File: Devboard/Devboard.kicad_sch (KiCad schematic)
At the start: 49 parts, among them IC1 114993390, J1 693071010811, J2 USB_C_Receptacle_USB2.0_16P, J3 SWD, J4 RMF, J5 RMF, SW1 SHPHLD, SW2 SW_Push, SW3 RST, U1 NPM1304-QEAA-R, U2 E73-2G4M08S1C, U3 SRV05-4, Y1 32.768

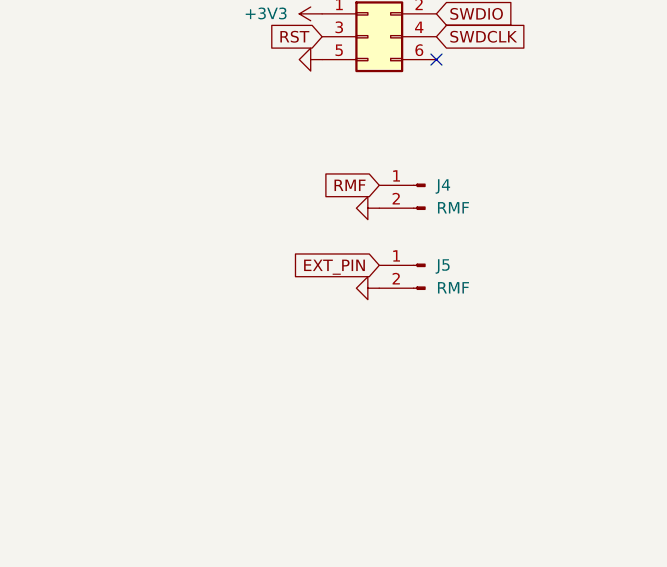
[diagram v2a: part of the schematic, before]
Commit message: Added 3V3 output
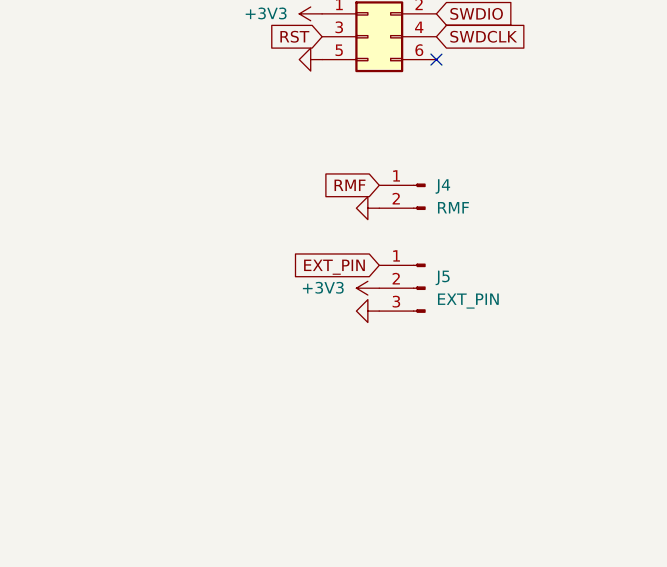
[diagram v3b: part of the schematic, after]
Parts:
- removed J5: RMF, Connector_PinHeader_2.54mm:PinHeader_1x02_P2.54mm_Vertical, symbol Connector:Conn_01x02_Pin
- added J5: EXT_PIN, Connector_PinHeader_2.54mm:PinHeader_1x03_P2.54mm_Vertical, symbol Connector:Conn_01x03_Pin
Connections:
- net +3V3: now also J5.2 (Pin_2)
- net EXT_PIN: now also J5.1 (Pin_1)
- net GND: now also J5.3 (Pin_3)
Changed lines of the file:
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@@
+	)
+	(symbol
+		(lib_id "power:+3.3V")
+		(at 372.11 142.24 90)
+		(unit 1)
+		(body_style 1)
+		(exclude_from_sim no)
+		(in_bom yes)
+		(on_board yes)
+		(in_pos_files yes)
+		(dnp no)
+		(fields_autoplaced yes)
+		(property "Reference" "#PWR048"
+			(at 375.92 142.24 0)
+			(hide yes)
+			(show_name no)
+			(do_not_autoplace no)
+			(effects
+				(font
+					(size 1.27 1.27)
+				)
+			)
+		)
+		(property "Value" "+3V3"
+			(at 368.3 142.2399 90)
+			(show_name no)
+			(do_not_autoplace no)
+			(effects
+				(font
+					(size 1.27 1.27)
+				)
+				(justify left)
+			)
+		)
+		(property "Footprint" ""
+			(at 372.11 142.24 0)
+			(hide yes)
+			(show_name no)
+			(do_not_autoplace no)
+			(effects
+				(font
+					(size 1.27 1.27)
+				)
+			)
+		)
+		(property "Datasheet" ""
+			(at 372.11 142.24 0)
+			(hide yes)
+			(show_name no)
+			(do_not_autoplace no)
+			(effects
+				(font
+					(size 1.27 1.27)
+				)
+			)
+		)
+		(property "Description" "Power symbol creates a global label with name \"+3.3V\""
+			(at 372.11 142.24 0)
+			(hide yes)
+			(show_name no)
+			(do_not_autoplace no)
+			(effects
+				(font
+					(size 1.27 1.27)
+				)
+			)
+		)
+		(pin "1"
+		)
+		(instances
+			(project "Devboard"
+				(path "/0a0a1e18-e167-488d-99d1-7fc114522a17"
+					(reference "#PWR048")
+					(unit 1)
+				)
+			)
+		)
 	)
 	(symbol
@@
 	(symbol
 		(lib_id "power:GND")
-		(at 372.11 142.24 270)
+		(at 372.11 144.78 270)
 		(unit 1)
 		(body_style 1)
@@
 		(dnp no)
 		(property "Reference" "#PWR047"
-			(at 365.76 142.24 0)
+			(at 365.76 144.78 0)
 			(hide yes)
 			(show_name no)
@@
 		)
 		(property "Value" "GND"
-			(at 368.8588 142.367 90)
+			(at 368.8588 144.907 90)
 			(hide yes)
 			(show_name no)
@@
 		)
 		(property "Footprint" ""
-			(at 372.11 142.24 0)
-			(hide yes)
-			(show_name no)
-			(do_not_autoplace no)
-			(effects
-				(font
-					(size 1.27 1.27)
-				)
-			)
-		)
-		(property "Datasheet" ""
-			(at 372.11 142.24 0)
+			(at 372.11 144.78 0)
+			(hide yes)
+			(show_name no)
+			(do_not_autoplace no)
+			(effects
+				(font
+					(size 1.27 1.27)
+				)
+			)
+		)
+		(property "Datasheet" ""
+			(at 372.11 144.78 0)
 			(hide yes)
 			(show_name no)
@@
 		)
 		(property "Description" ""
-			(at 372.11 142.24 0)
+			(at 372.11 144.78 0)
 			(show_name no)
 			(do_not_autoplace no)
@@
 	)
 	(symbol
+		(lib_id "Connector:Conn_01x03_Pin")
+		(at 377.19 142.24 0)
+		(mirror y)
+		(unit 1)
+		(body_style 1)
+		(exclude_from_sim no)
+		(in_bom yes)
+		(on_board yes)
+		(in_pos_files yes)
+		(dnp no)
+		(fields_autoplaced yes)
+		(property "Reference" "J5"
+			(at 378.46 140.9699 0)
+			(show_name no)
+			(do_not_autoplace no)
+			(effects
+				(font
+					(size 1.27 1.27)
+				)
+				(justify right)
+			)
+		)
+		(property "Value" "EXT_PIN"
+			(at 378.46 143.5099 0)
+			(show_name no)
+			(do_not_autoplace no)
+			(effects
+				(font
+					(size 1.27 1.27)
+				)
+				(justify right)
+			)
+		)
+		(property "Footprint" "Connector_PinHeader_2.54mm:PinHeader_1x03_P2.54mm_Vertical"
+			(at 377.19 142.24 0)
+			(hide yes)
+			(show_name no)
+			(do_not_autoplace no)
+			(effects
+				(font
+					(size 1.27 1.27)
+				)
+			)
+		)
+		(property "Datasheet" ""
+			(at 377.19 142.24 0)
+			(hide yes)
+			(show_name no)
+			(do_not_autoplace no)
+			(effects
+				(font
+					(size 1.27 1.27)
+				)
+			)
+		)
+		(property "Description" "Generic connector, single row, 01x03, script generated"
+			(at 377.19 142.24 0)
+			(hide yes)
+			(show_name no)
+			(do_not_autoplace no)
+			(effects
+				(font
+					(size 1.27 1.27)
+				)
+			)
+		)
+		(pin "1"
+		)
+		(pin "3"
+		)
+		(pin "2"
+		)
+		(instances
+			(project "Devboard"
+				(path "/0a0a1e18-e167-488d-99d1-7fc114522a17"
+					(reference "J5")
+					(unit 1)
+				)
+			)
+		)
+	)
+	(symbol
 		(lib_id "Connector:Conn_01x02_Pin")
 		(at 377.19 130.81 0)
@@
 					(unit 1)
 				)
-			)
-		)
-	)
-	(symbol
-		(lib_id "Connector:Conn_01x02_Pin")
-		(at 377.19 139.7 0)
-		(mirror y)
-		(unit 1)
-		(body_style 1)
-		(exclude_from_sim no)
-		(in_bom yes)
-		(on_board yes)
-		(in_pos_files yes)
-		(dnp no)
-		(fields_autoplaced yes)
-		(property "Reference" "J5"
-			(at 378.46 139.6999 0)
-			(show_name no)
-			(do_not_autoplace no)
-			(effects
-				(font
-					(size 1.27 1.27)
-				)
-				(justify right)
-			)
-		)
-		(property "Value" "RMF"
-			(at 378.46 142.2399 0)
-			(show_name no)
-			(do_not_autoplace no)
-			(effects
-				(font
-					(size 1.27 1.27)
-				)
-				(justify right)
-			)
-		)
-		(property "Footprint" "Connector_PinHeader_2.54mm:PinHeader_1x02_P2.54mm_Vertical"
-			(at 377.19 139.7 0)
-			(hide yes)
-			(show_name no)
-			(do_not_autoplace no)
-			(effects
-				(font
-					(size 1.27 1.27)
-				)
-			)
-		)
-		(property "Datasheet" ""
-			(at 377.19 139.7 0)
-			(hide yes)
-			(show_name no)
-			(do_not_autoplace no)
-			(effects
-				(font
-					(size 1.27 1.27)
-				)
-			)
-		)
-		(property "Description" "Generic connector, single row, 01x02, script generated"
-			(at 377.19 139.7 0)
-			(hide yes)
-			(show_name no)
-			(do_not_autoplace no)
-			(effects
-				(font
-					(size 1.27 1.27)
-				)
-			)
-		)
-		(pin "1"
-		)
-		(pin "2"
-		)
-		(instances
-			(project "Devboard"
-				(path "/0a0a1e18-e167-488d-99d1-7fc114522a17"
-					(reference "J5")
-					(unit 1)
-				)

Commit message: Final commit
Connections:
- net +3V3 is gone; now on net +3.3V: J3.1 (Pin_1), J5.2 (Pin_2)
- no-connect marks 24 -> 26
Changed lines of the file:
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@@
 	)
 	(junction
+		(at 161.29 69.85)
+		(diameter 0)
+		(color 0 0 0 0)
+	)
+	(junction
 		(at 312.42 29.21)
 		(diameter 0)
@@
 	)
 	(junction
-		(at 161.29 69.85)
-		(diameter 0)
-		(color 0 0 0 0)
-	)
-	(junction
 		(at 243.84 223.52)
 		(diameter 0)
@@
 	)
 	(no_connect
+		(at 387.35 41.91)
+	)
+	(no_connect
 		(at 302.26 205.74)
 	)
@@
 	)
 	(no_connect
+		(at 73.66 199.39)
+	)
+	(no_connect
 		(at 67.31 57.15)
 	)
@@
 	(wire
 		(pts
-			(xy 161.29 63.5) (xy 161.29 69.85)
+			(xy 161.29 64.77) (xy 161.29 69.85)
 		)
 		(stroke
@@
 	)
 	(label "PVDD"
-		(at 161.29 63.5 270)
+		(at 161.29 64.77 270)
 		(effects
 			(font
@@
 	)
 	(symbol
-		(lib_id "power:+3.3V")
-		(at 372.11 142.24 90)
-		(unit 1)
-		(body_style 1)
-		(exclude_from_sim no)
-		(in_bom yes)
-		(on_board yes)
-		(in_pos_files yes)
-		(dnp no)
-		(fields_autoplaced yes)
-		(property "Reference" "#PWR048"
-			(at 375.92 142.24 0)
-			(hide yes)
-			(show_name no)
-			(do_not_autoplace no)
-			(effects
-				(font
-					(size 1.27 1.27)
-				)
-			)
-		)
-		(property "Value" "+3V3"
-			(at 368.3 142.2399 90)
-			(show_name no)
-			(do_not_autoplace no)
-			(effects
-				(font
-					(size 1.27 1.27)
-				)
-				(justify left)
-			)
-		)
-		(property "Footprint" ""
-			(at 372.11 142.24 0)
-			(hide yes)
-			(show_name no)
-			(do_not_autoplace no)
-			(effects
-				(font
-					(size 1.27 1.27)
-				)
-			)
-		)
-		(property "Datasheet" ""
-			(at 372.11 142.24 0)
-			(hide yes)
-			(show_name no)
-			(do_not_autoplace no)
-			(effects
-				(font
-					(size 1.27 1.27)
-				)
-			)
-		)
-		(property "Description" "Power symbol creates a global label with name \"+3.3V\""
-			(at 372.11 142.24 0)
-			(hide yes)
-			(show_name no)
-			(do_not_autoplace no)
-			(effects
-				(font
-					(size 1.27 1.27)
-				)
-			)
-		)
-		(pin "1"
-		)
-		(instances
-			(project "Devboard"
-				(path "/0a0a1e18-e167-488d-99d1-7fc114522a17"
-					(reference "#PWR048")
-					(unit 1)
-				)
-			)
-		)
-	)
-	(symbol
 		(lib_id "power:VBUS")
 		(at 283.21 184.15 270)
@@
 	)
 	(symbol
-		(lib_id "power:+3.3V")
-		(at 365.76 111.76 90)
-		(unit 1)
-		(body_style 1)
-		(exclude_from_sim no)
-		(in_bom yes)
-		(on_board yes)
-		(in_pos_files yes)
-		(dnp no)
-		(fields_autoplaced yes)
-		(property "Reference" "#PWR042"
-			(at 369.57 111.76 0)
-			(hide yes)
-			(show_name no)
-			(do_not_autoplace no)
-			(effects
-				(font
-					(size 1.27 1.27)
-				)
-			)
-		)
-		(property "Value" "+3V3"
-			(at 361.95 111.7599 90)
-			(show_name no)
-			(do_not_autoplace no)
-			(effects
-				(font
-					(size 1.27 1.27)
-				)
-				(justify left)
-			)
-		)
-		(property "Footprint" ""
-			(at 365.76 111.76 0)
-			(hide yes)
-			(show_name no)
-			(do_not_autoplace no)
-			(effects
-				(font
-					(size 1.27 1.27)
-				)
-			)
-		)
-		(property "Datasheet" ""
-			(at 365.76 111.76 0)
-			(hide yes)
-			(show_name no)
-			(do_not_autoplace no)
-			(effects
-				(font
-					(size 1.27 1.27)
-				)
-			)
-		)
-		(property "Description" "Power symbol creates a global label with name \"+3.3V\""
-			(at 365.76 111.76 0)
-			(hide yes)
-			(show_name no)
-			(do_not_autoplace no)
-			(effects
-				(font
-					(size 1.27 1.27)
-				)
-			)
-		)
-		(pin "1"
-		)
-		(instances
-			(project "Devboard"
-				(path "/0a0a1e18-e167-488d-99d1-7fc114522a17"
-					(reference "#PWR042")
-					(unit 1)
-				)
-			)
-		)
-	)
-	(symbol
 		(lib_id "Device:R_Small")
 		(at 160.02 54.61 90)
@@
 	(symbol
 		(lib_id "power:+3.3V")
+		(at 365.76 111.76 90)
+		(unit 1)
+		(body_style 1)
+		(exclude_from_sim no)
+		(in_bom yes)
+		(on_board yes)
+		(in_pos_files yes)
+		(dnp no)
+		(fields_autoplaced yes)
+		(property "Reference" "#PWR042"
+			(at 369.57 111.76 0)
+			(hide yes)
+			(show_name no)
+			(do_not_autoplace no)
+			(effects
+				(font
+					(size 1.27 1.27)
+				)
+			)
+		)
+		(property "Value" "+3.3V"
+			(at 361.95 111.7599 90)
+			(show_name no)
+			(do_not_autoplace no)
+			(effects
+				(font
+					(size 1.27 1.27)
+				)
+				(justify left)
+			)
+		)
+		(property "Footprint" ""
+			(at 365.76 111.76 0)
+			(hide yes)
+			(show_name no)
+			(do_not_autoplace no)
+			(effects
+				(font
+					(size 1.27 1.27)
+				)
+			)
+		)
+		(property "Datasheet" ""
+			(at 365.76 111.76 0)
+			(hide yes)
+			(show_name no)
+			(do_not_autoplace no)
+			(effects
+				(font
+					(size 1.27 1.27)
+				)
+			)
+		)
+		(property "Description" "Power symbol creates a global label with name \"+3.3V\""
+			(at 365.76 111.76 0)
+			(hide yes)
+			(show_name no)
+			(do_not_autoplace no)
+			(effects
+				(font
+					(size 1.27 1.27)
+				)
+			)
+		)
+		(pin "1"
+		)
+		(instances
+			(project "Devboard"
+				(path "/0a0a1e18-e167-488d-99d1-7fc114522a17"
+					(reference "#PWR042")
+					(unit 1)
+				)
+			)
+		)
+	)
+	(symbol
+		(lib_id "power:+3.3V")
 		(at 226.06 41.91 180)
 		(unit 1)
@@
 					(unit 1)
 				)
+			)
+		)
+	)
+	(symbol
+		(lib_id "power:+3.3V")
+		(at 372.11 142.24 90)
+		(unit 1)
+		(body_style 1)
+		(exclude_from_sim no)
+		(in_bom yes)
+		(on_board yes)
+		(in_pos_files yes)
+		(dnp no)
+		(fields_autoplaced yes)
+		(property "Reference" "#PWR048"
+			(at 375.92 142.24 0)
+			(hide yes)
+			(show_name no)
+			(do_not_autoplace no)
+			(effects
+				(font
+					(size 1.27 1.27)
+				)
+			)
+		)
+		(property "Value" "+3.3V"
+			(at 368.3 142.2399 90)
+			(show_name no)
+			(do_not_autoplace no)
+			(effects
+				(font
+					(size 1.27 1.27)
+				)
+				(justify left)
+			)
+		)
+		(property "Footprint" ""
+			(at 372.11 142.24 0)
+			(hide yes)
+			(show_name no)
+			(do_not_autoplace no)
+			(effects
+				(font
+					(size 1.27 1.27)
+				)
+			)
+		)
+		(property "Datasheet" ""
+			(at 372.11 142.24 0)
+			(hide yes)
+			(show_name no)
+			(do_not_autoplace no)
+			(effects
+				(font
+					(size 1.27 1.27)
+				)
+			)
+		)
+		(property "Description" "Power symbol creates a global label with name \"+3.3V\""
+			(at 372.11 142.24 0)
+			(hide yes)
+			(show_name no)
+			(do_not_autoplace no)
+			(effects
+				(font
+					(size 1.27 1.27)
+				)
+			)
+		)
+		(pin "1"
+		)
+		(instances
+			(project "Devboard"
+				(path "/0a0a1e18-e167-488d-99d1-7fc114522a17"
+					(reference "#PWR048")
+					(unit 1)
+				)
